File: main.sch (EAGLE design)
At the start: 42 parts

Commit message: Added lib folder, added charge controller schematic
Almost finished naming nets and component values.
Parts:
- removed STATUS0, STATUS4: (no value), pinhead:PINHD-1X2
- added BATT: (no value), pinhead:PINHD-1X2
- added C11, C21, C23: 1u, resistor:C-USC0603
- added C12: 2.2u, resistor:C-USC0603
- added C13, C14, C16, C18, C22: 100n, resistor:C-USC0603
- added C15, C19, C20: 10u, resistor:C-USC0603
- added C17: 47n, resistor:C-USC0603
- added C9: 100nF, resistor:C-USC0603
- added D1: BAS70-05, diode:BAS70-05
- added L2: 3.3u, resistor:L-USL2012C
- added LED1: (no value), adafruit:LEDCHIPLED_0603
- added Q1, Q2: 5.8A/30V/35mΩ, SparkFun-DiscreteSemi:MOSFET-NCH-AO3404A
- added Q3: 2.5A/30V/105mΩ, SparkFun-DiscreteSemi:MOSFET_PCH-DMG2307L
- added R10: 2, resistor:R-US_R0603
- added R11, R12: 4.02k, resistor:R-US_R0603
- added R13: 20m, resistor:R-US_R0603
- added R23, R33: 0, resistor:R-US_R0603
- added R26: 1k, resistor:R-US_R0603
- added R27: 10m, resistor:R-US_R0603
- added R28: 232k, resistor:R-US_R0603
- added R29, R35: 32.4k, resistor:R-US_R0603
- added R30: 5.23k, resistor:R-US_R0603
- added R31: 30.1k, resistor:R-US_R0603
- added R32: 1.5k, resistor:R-US_R0603
- added R34, R9: 100k, resistor:R-US_R0603
- added R7: 10, resistor:R-US_R0603
- added R8: 1M, resistor:R-US_R0603
- added RS-485: (no value), pinhead:PINHD-1X4
- added R_THERM: 103AT, pinhead:PINHD-1X2
- added S1: (no value), switch:M251
- added U2: SN65HVD32_D_8, SN65HVD32:SN65HVD32_D_8
- renumbered STATUS1 to V1, STATUS2 to V2, STATUS3 to V0
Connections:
- removed net GPIO_IN_3: V0.2
- removed net GPIO_IN_4: STATUS4.2
- new net MCU_RX: U2.D
- new net MCU_TX: U2.R
- new net N$11: RS-485.2, U2.B
- new net N$12: RS-485.3, U2.Z
- new net N$13: RS-485.4, U2.Y
- new net N$14: D1.C, R7.1
- new net N$15: C12.1, R10.1
- new net N$16: Q1.S, Q2.S, R11.1
- new net N$17: Q1.G, Q2.G, R12.2
- new net N$19: Q3.G, R26.2
- new net N$20: LED1.A, R32.2
- new net N$6: RS-485.1, U2.A
- new net PC_ACDRV: POWER_CONTROLLER.ACDRV, R12.1
- new net PC_ACN: C13.2, C14.1, R13.1, R23.2
- new net PC_ACP: C13.1, POWER_CONTROLLER.ACP, Q2.D, R13.2
- new net PC_ACSET: POWER_CONTROLLER.ACSET, R34.2, R35.1
- new net PC_AVCC: C11.1, POWER_CONTROLLER.AVCC, R7.2
- new net PC_BTST: C17.2, POWER_CONTROLLER.BTST
- new net PC_CAN: POWER_CONTROLLER.CAN
- new net PC_CELL: POWER_CONTROLLER.CELL, R33.2
- new net PC_CMSRC: POWER_CONTROLLER.CMSRC, R11.2
- new net PC_ISET: POWER_CONTROLLER.ISET, R28.1, R29.2
- new net PC_NBATDRV: POWER_CONTROLLER.*BATDRV, R26.1
- new net PC_OVPSET: POWER_CONTROLLER.OVPSET, R8.1, R9.2
- new net PC_PVCC: C15.1, POWER_CONTROLLER.PVCC, POWER_CONTROLLER.PVCC_2, Q3.S, R23.1, S1.P
- new net PC_REGN: C23.1, POWER_CONTROLLER.REGN
- new net PC_SRN: BATT.1, C16.1, C19.1, C20.1, POWER_CONTROLLER.SRN, Q3.D, R27.1
- new net PC_SRP: C16.2, C18.1, L2.2, POWER_CONTROLLER.SRP, R27.2
- new net PC_STAT: LED1.C, POWER_CONTROLLER.STAT
- new net PC_SW: C17.1, L2.1, POWER_CONTROLLER.SW, POWER_CONTROLLER.SW_2
- new net PC_TS: POWER_CONTROLLER.TS, R30.2, R31.1, R_THERM.1
- new net PC_TTC: C22.1, POWER_CONTROLLER.TTC
- new net PC_VREF: C21.1, POWER_CONTROLLER.VREF, R28.2, R30.1, R32.1, R33.1, R34.1
- new net VSYS: 3.3V_REG.EN, 3.3V_REG.VIN, AIN0.1, AIN1.1, AIN2.1, AIN3.1, AIN4.1, C7.1, R4.1, S1.S
- new net V_BATT: D1.A1
- net 3.3V: now also C9.1, U2.VCC; no longer R4.1
- net D_STATE: no longer STATUS0.1, STATUS4.1
- net GND: now also BATT.2, C11.2, C12.2, C14.2, C15.2, C18.2, C19.2, C20.2, C21.2, C22.2, C23.2, C9.2, POWER_CONTROLLER.EPAD, POWER_CONTROLLER.PGND, POWER_CONTROLLER.PGND_2, R29.1, R31.2, R35.2, R9.1, R_THERM.2, U2.GND
- net GPIO_IN_0: now also V0.2; no longer STATUS0.2
- net VIN: now also D1.A2, Q1.D, R10.2, R8.2; no longer 3.3V_REG.EN, 3.3V_REG.VIN, AIN0.1, AIN1.1, AIN2.1, AIN3.1, AIN4.1, C7.1

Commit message: Added and removed some i/o
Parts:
- removed AIN0, AIN1, AIN2, AIN3, AIN4, D_STATE_JUMPER: (no value), pinhead:PINHD-1X3
- removed V0, V1, V2: (no value), pinhead:PINHD-1X2
- added 3.3V, PVCC: (no value), pinhead:PINHD-1X2
- added AIN: (no value), pinhead:PINHD-1X5
- added GPIO: (no value), pinhead:PINHD-1X3
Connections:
- net PA02_AIN0 renamed AIN0
- net PA04_AIN4 renamed AIN1
- net PA05_AIN5 renamed AIN2
- net PB08_AIN2 renamed AIN3
- net PB09_AIN3 renamed AIN4
- removed net D_STATE: D_STATE_JUMPER.2, V0.1, V1.1, V2.1
- removed net GPIO_IN_0: V0.2
- removed net GPIO_IN_1: V1.2
- removed net GPIO_IN_2: V2.2
- new net GPIO1: GPIO.1
- new net GPIO2: GPIO.2
- new net GPIO3: GPIO.3
- net 3.3V: now also 3.3V.1, R4.1; no longer D_STATE_JUMPER.1
- net GND: now also 3.3V.2, PVCC.2; no longer AIN0.2, AIN1.2, AIN2.2, AIN3.2, AIN4.2, D_STATE_JUMPER.3
- net N$1: now also AIN.2; no longer AIN1.3
- net N$3: now also AIN.3; no longer AIN2.3
- net N$4: now also AIN.4; no longer AIN3.3
- net N$5: now also AIN.5; no longer AIN4.3
- net N$8: now also AIN.1; no longer AIN0.3
- net VSYS: now also PVCC.1; no longer AIN0.1, AIN1.1, AIN2.1, AIN3.1, AIN4.1, R4.1

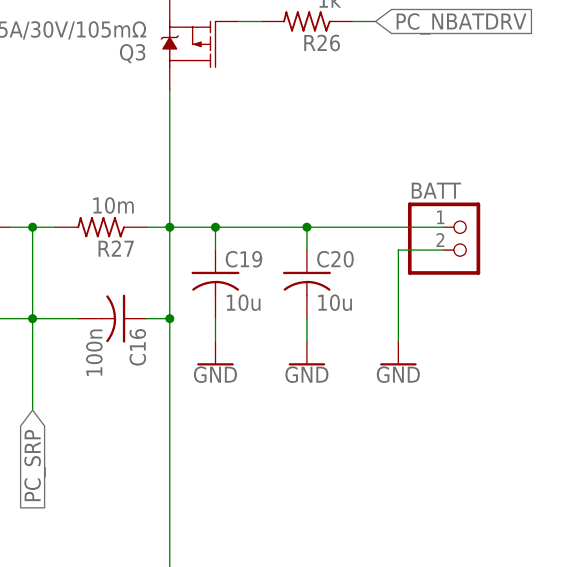
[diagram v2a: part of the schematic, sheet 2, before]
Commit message: Started board design
Still need to add I2C, GPIO, and AIO nets in schematic. Need to also add status leds.
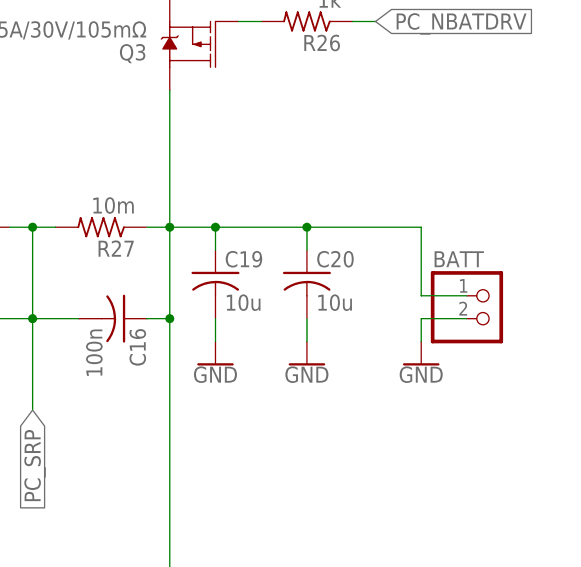
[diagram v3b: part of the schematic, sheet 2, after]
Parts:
- added VCHG: (no value), pinhead:PINHD-1X2
- renumbered PVCC to VDUC
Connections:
- net GND: now also VCHG.2
- net MCU_RX: now also SAMD21G18A.PB23(SER5:3+)
- net MCU_TX: now also SAMD21G18A.PB22(SER5:2+)
- net VIN: now also VCHG.1
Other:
- moved on the sheet: BATT
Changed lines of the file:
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@@
 <part name="AIN" library="pinhead" library_urn="urn:adsk.eagle:library:325" deviceset="PINHD-1X5" device="" package3d_urn="urn:adsk.eagle:package:22469/2"/>
 <part name="GPIO" library="pinhead" library_urn="urn:adsk.eagle:library:325" deviceset="PINHD-1X3" device="" package3d_urn="urn:adsk.eagle:package:22458/2"/>
-<part name="PVCC" library="pinhead" library_urn="urn:adsk.eagle:library:325" deviceset="PINHD-1X2" device="" package3d_urn="urn:adsk.eagle:package:22435/2"/>
+<part name="VDUC" library="pinhead" library_urn="urn:adsk.eagle:library:325" deviceset="PINHD-1X2" device="" package3d_urn="urn:adsk.eagle:package:22435/2"/>
 <part name="3.3V" library="pinhead" library_urn="urn:adsk.eagle:library:325" deviceset="PINHD-1X2" device="" package3d_urn="urn:adsk.eagle:package:22435/2"/>
 <part name="GND4" library="SparkFun-PowerSymbols" deviceset="GND" device=""/>
 <part name="GND19" library="SparkFun-PowerSymbols" deviceset="GND" device=""/>
 <part name="SUPPLY8" library="SparkFun-PowerSymbols" deviceset="3.3V" device=""/>
+<part name="VCHG" library="pinhead" library_urn="urn:adsk.eagle:library:325" deviceset="PINHD-1X2" device="" package3d_urn="urn:adsk.eagle:package:22435/2"/>
+<part name="GND21" library="SparkFun-PowerSymbols" deviceset="GND" device=""/>
+<part name="SUPPLY9" library="SparkFun-PowerSymbols" deviceset="VIN" device=""/>
 </parts>
 <sheets>
@@
 <instance part="AIN" gate="A" x="429.26" y="119.38"/>
 <instance part="GPIO" gate="A" x="393.7" y="139.7"/>
-<instance part="PVCC" gate="G$1" x="393.7" y="165.1"/>
+<instance part="VDUC" gate="G$1" x="393.7" y="165.1"/>
 <instance part="3.3V" gate="G$1" x="393.7" y="182.88"/>
 <instance part="GND4" gate="1" x="373.38" y="160.02"/>
 <instance part="GND19" gate="1" x="373.38" y="177.8"/>
 <instance part="SUPPLY8" gate="G$1" x="373.38" y="187.96"/>
+<instance part="VCHG" gate="G$1" x="424.18" y="182.88"/>
+<instance part="GND21" gate="1" x="403.86" y="177.8"/>
+<instance part="SUPPLY9" gate="G$1" x="403.86" y="187.96"/>
 </instances>
 <busses>
@@
 </segment>
 <segment>
-<pinref part="PVCC" gate="G$1" pin="2"/>
+<pinref part="VDUC" gate="G$1" pin="2"/>
 <wire x1="391.16" y1="165.1" x2="373.38" y2="165.1" width="0.1524" layer="91"/>
 <wire x1="373.38" y1="165.1" x2="373.38" y2="162.56" width="0.1524" layer="91"/>
@@
 <wire x1="373.38" y1="182.88" x2="373.38" y2="180.34" width="0.1524" layer="91"/>
 <pinref part="GND19" gate="1" pin="GND"/>
+</segment>
+<segment>
+<pinref part="VCHG" gate="G$1" pin="2"/>
+<wire x1="421.64" y1="182.88" x2="403.86" y2="182.88" width="0.1524" layer="91"/>
+<wire x1="403.86" y1="182.88" x2="403.86" y2="180.34" width="0.1524" layer="91"/>
+<pinref part="GND21" gate="1" pin="GND"/>
 </segment>
 </net>
@@
 <label x="457.2" y="86.36" size="1.778" layer="95"/>
 </segment>
+<segment>
+<pinref part="SAMD21G18A" gate="G$1" pin="PB22(SER5:2+)"/>
+<wire x1="203.2" y1="60.96" x2="223.52" y2="60.96" width="0.1524" layer="91"/>
+<label x="205.74" y="60.96" size="1.778" layer="95"/>
+</segment>
 </net>
 <net name="MCU_RX" class="0">
@@
 <wire x1="467.36" y1="83.82" x2="457.2" y2="83.82" width="0.1524" layer="91"/>
 <label x="457.2" y="83.82" size="1.778" layer="95"/>
+</segment>
+<segment>
+<pinref part="SAMD21G18A" gate="G$1" pin="PB23(SER5:3+)"/>
+<wire x1="203.2" y1="58.42" x2="223.52" y2="58.42" width="0.1524" layer="91"/>
+<label x="205.74" y="58.42" size="1.778" layer="95"/>
 </segment>
 </net>
@@
 <net name="VSYS" class="0">
 <segment>
-<pinref part="PVCC" gate="G$1" pin="1"/>
+<pinref part="VDUC" gate="G$1" pin="1"/>
 <wire x1="391.16" y1="167.64" x2="373.38" y2="167.64" width="0.1524" layer="91"/>
 <label x="373.38" y="167.64" size="1.778" layer="95"/>
+</segment>
+</net>
+<net name="VIN" class="0">
+<segment>
+<pinref part="VCHG" gate="G$1" pin="1"/>
+<wire x1="421.64" y1="185.42" x2="403.86" y2="185.42" width="0.1524" layer="91"/>
+<wire x1="403.86" y1="185.42" x2="403.86" y2="187.96" width="0.1524" layer="91"/>
+<pinref part="SUPPLY9" gate="G$1" pin="VIN"/>
 </segment>
 </net>
@@
 <instance part="GND31" gate="1" x="469.9" y="43.18"/>
 <instance part="GND32" gate="1" x="480.06" y="43.18"/>
-<instance part="BATT" gate="G$1" x="497.84" y="55.88"/>
-<instance part="GND33" gate="1" x="490.22" y="43.18"/>
+<instance part="BATT" gate="G$1" x="500.38" y="48.26"/>
+<instance part="GND33" gate="1" x="492.76" y="43.18"/>
 <instance part="R28" gate="G$1" x="248.92" y="10.16" rot="R90"/>
 <instance part="R29" gate="G$1" x="248.92" y="-5.08" rot="R90"/>
@@
 <segment>
 <pinref part="BATT" gate="G$1" pin="2"/>
-<wire x1="495.3" y1="55.88" x2="490.22" y2="55.88" width="0.1524" layer="91"/>
-<wire x1="490.22" y1="55.88" x2="490.22" y2="45.72" width="0.1524" layer="91"/>
+<wire x1="497.84" y1="48.26" x2="492.76" y2="48.26" width="0.1524" layer="91"/>
+<wire x1="492.76" y1="48.26" x2="492.76" y2="45.72" width="0.1524" layer="91"/>
 <pinref part="GND33" gate="1" pin="GND"/>
 </segment>
@@
 <pinref part="C20" gate="G$1" pin="1"/>
 <wire x1="480.06" y1="58.42" x2="480.06" y2="55.88" width="0.1524" layer="91"/>
-<wire x1="480.06" y1="58.42" x2="495.3" y2="58.42" width="0.1524" layer="91"/>
+<wire x1="480.06" y1="58.42" x2="492.76" y2="58.42" width="0.1524" layer="91"/>
+<wire x1="492.76" y1="58.42" x2="492.76" y2="50.8" width="0.1524" layer="91"/>
 <junction x="480.06" y="58.42"/>
 <pinref part="BATT" gate="G$1" pin="1"/>
-</segment>
-</net>
+<wire x1="492.76" y1="50.8" x2="497.84" y2="50.8" width="0.1524" layer="91"/>
+</segment>
+</net>

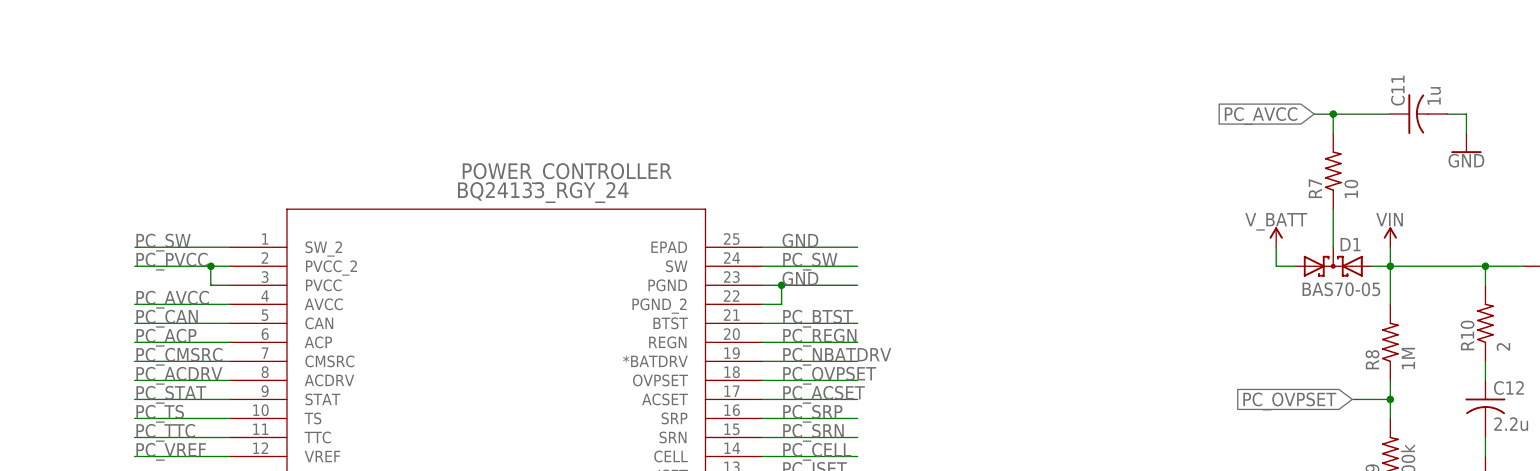
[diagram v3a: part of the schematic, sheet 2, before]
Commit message: Assembled alot of the board layout
Mostly charge controller elements
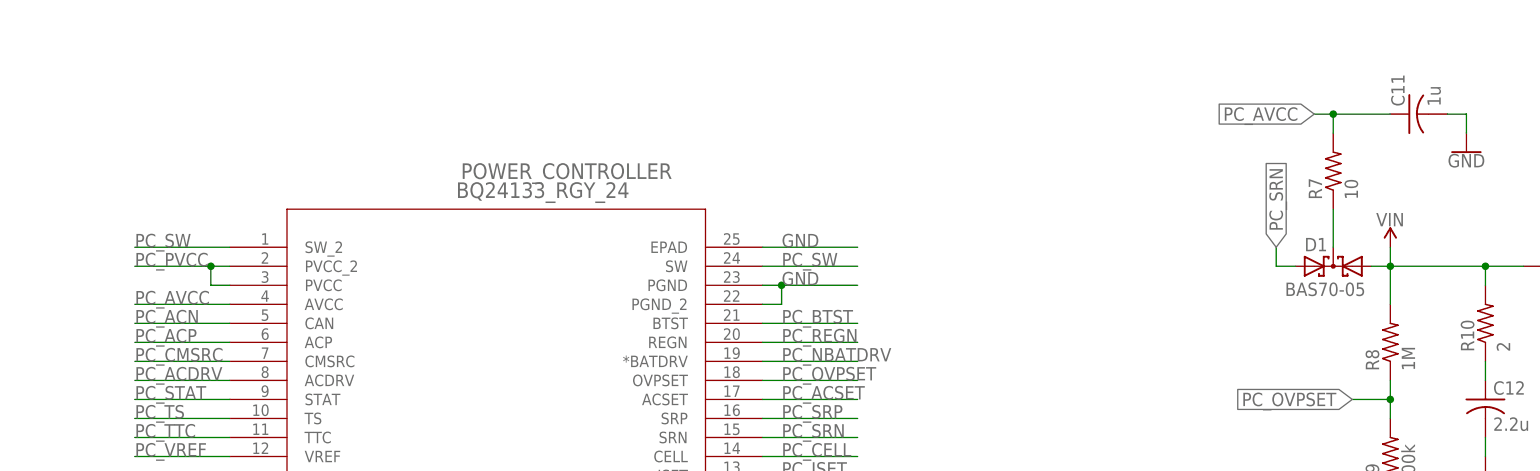
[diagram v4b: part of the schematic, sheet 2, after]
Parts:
- C11, C12, C14, C15, C18, C19, C20, C7: device resistor:C-USC0603 -> rcl:C-USC1206
- renumbered 3.3V to GND
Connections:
- removed net PC_CAN: POWER_CONTROLLER.CAN
- removed net V_BATT: D1.A1
- net 3.3V: no longer GND.1
- net GND: now also GND.1
- net PC_ACN: now also POWER_CONTROLLER.CAN
- net PC_SRN: now also D1.A2
- net VIN: now also D1.A1; no longer D1.A2
